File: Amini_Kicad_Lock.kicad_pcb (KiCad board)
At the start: 2 copper layers, 25.7 x 19.1 mm, 40 parts, among them J1 Conn_01x02_Pin, J2 Conn_01x04, J3 MM8130-2600RA2, J4 Conn_01x03_Pin, U1 nRF5340-QKxx, X1 32MHz, X2 32.768kHz

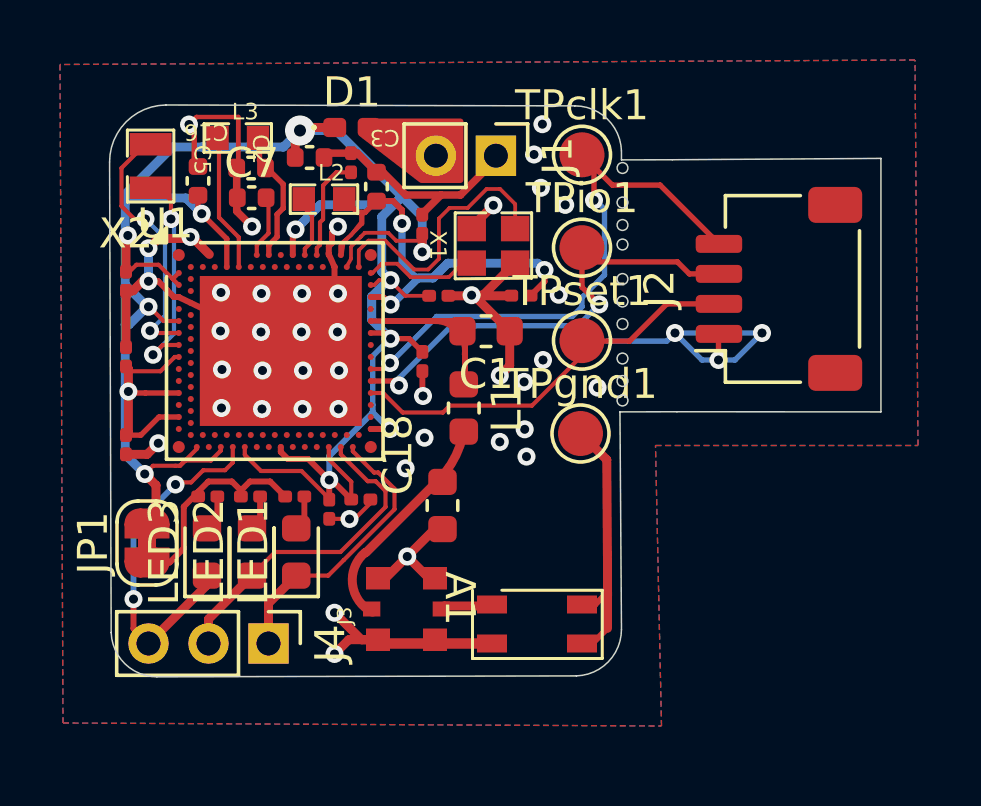
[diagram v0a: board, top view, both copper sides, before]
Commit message: New antenna design done
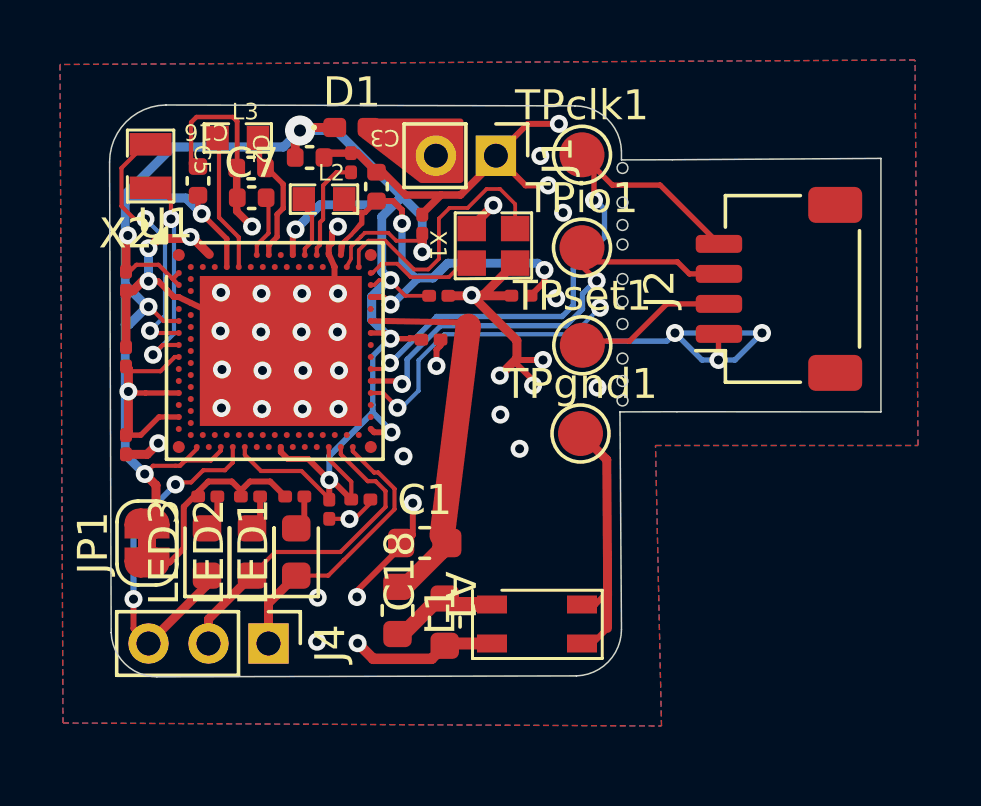
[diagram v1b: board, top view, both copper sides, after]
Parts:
- removed J3: MM8130-2600RA2, MM8130-2600RA2 antenna:MURATA_MM8130-2600RA2
- moved C1 7.35 mm to (182.2, 68.2), turned to 0 degrees
- moved L1 7.10 mm to (181.3, 70.5)
- moved C18 3.89 mm to (182.9, 70.9)
- moved C13 0.43 mm to (182.1, 61.5), turned to 0 degrees
- moved TPset1 0.16 mm to (187.5, 61.7)
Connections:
- A1 pad 1: Net-(A1-Pad1) -> Net-(C18-Pad2)
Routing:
- net GND: track 66.3 -> 70.6 mm, vias 47 -> 46
- net Net-(U1-ANT): track 0.00 -> 2.45 mm
- net Net-(A1-Pad1): track 1.75 -> 0.00 mm
- net /~{RESET}: track 13.4 -> 15.1 mm, vias 0 -> 2

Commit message: some changes done
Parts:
- removed J4: Conn_01x03_Pin, Connector_PinHeader_2.00mm:PinHeader_1x03_P2.00mm_Vertical
- added C17: 0.7pF, Capacitor_SMD:C_0402_1005Metric_Pad0.74x0.62mm_HandSolder, F.Cu at (183.4, 61.4)
- added C19: N.C., Capacitor_SMD:C_0402_1005Metric_Pad0.74x0.62mm_HandSolder, F.Cu at (185.4, 63.0)
- added J3: Conn_01x04_Pin, Connector_PinHeader_2.00mm:PinHeader_1x04_P2.00mm_Vertical, F.Cu at (180.1, 71.5)
- added L4: 2.2nH, Capacitor_SMD:C_0402_1005Metric_Pad0.74x0.62mm_HandSolder, F.Cu at (184.9, 61.2)
- C1, C18, L1: footprint Inductor_SMD:L_0603_1608Metric -> Capacitor_SMD:C_0402_1005Metric_Pad0.74x0.62mm_HandSolder
- J2: footprint Connector_JST:JST_SH_SM04B-SRSS-TB_1x04-1MP_P1.00mm_Horizontal -> Connector_PinHeader_2.54mm:PinHeader_2x02_P2.54mm_Vertical
- moved C18 3.68 mm to (182.8, 67.2), turned to 180 degrees
- moved C1 2.60 mm to (182.9, 70.8), turned to 60 degrees
- moved J2 2.11 mm to (192.1, 60.6)
- moved L1 1.90 mm to (182.2, 68.8), turned to -70 degrees
- moved C14 0.31 mm to (182.1, 59.9)
- moved C13 0.11 mm to (182.0, 61.5), turned to -90 degrees
- moved C11 0.11 mm to (179.0, 67.0)
- moved J1 0.06 mm to (184.6, 55.3)
- renumbered TPclk1 to clk, TPgnd1 to gnd, TPio1 to io, TPset1 to set
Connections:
- C1 pad 2: Net-(U1-ANT) -> Net-(C1-Pad2)
- L1 pad 1: Net-(U1-ANT) -> Net-(C1-Pad2)
- LED1 pad 1: /LED1 -> /LED3
- LED3 pad 1: /LED3 -> /LED1
- U1 pad A25: GND -> unconnected-(U1-NC-PadA25)
- U1 pad AA1: unconnected-(U1-NFC2/P0.03-PadAA1) -> /MIC
- U1 pad AE31: (no net) -> unconnected-(U1-AIN7/P0.28-PadAE31)
- U1 pad AL29: /LED1 -> /LED3
- U1 pad AL9: /LED3 -> unconnected-(U1-IO3/P0.16-PadAL9)
- U1 pad B26: GND -> unconnected-(U1-NC-PadB26)
- U1 pad G1: GND -> unconnected-(U1-NC-PadG1)
- U1 pad H2: GND -> unconnected-(U1-NC-PadH2)
- U1 pad W1: unconnected-(U1-NFC1/P0.02-PadW1) -> /LED1
- X1 pad 4: GND -> unconnected-(X1-GND-Pad4)
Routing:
- net /MIC: track 0.00 -> 10.3 mm, vias 0 -> 1
- net /~{RESET}: track 15.1 -> 25.0 mm
- net GND: track 70.6 -> 61.5 mm, vias 46 -> 41
- net /LED1: track 9.57 -> 15.5 mm, vias 0 -> 1
- net Net-(A1-Pad1): track 3.71 -> 0.00 mm
- net /SWDIO: track 15.6 -> 19.0 mm
- net /SWDCLK: track 19.2 -> 21.4 mm
- net /LED3: track 11.9 -> 10.0 mm, vias 2 -> 0
- net Net-(U1-ANT): track 2.45 -> 4.15 mm
- net VDD_nRF: track 85.5 -> 87.1 mm
- net unconnected-(X1-GND-Pad4): track 0.00 -> 1.08 mm
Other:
- board text added: "+"
- board text added: "2024 - June - v.1.0"
- board text added: "AMINI"
- board text added: "Bluetooth"
- board text added: "Lock"
- board text added: "clk"
- board text added: "gnd"
- board text added: "io"
- board text added: "set"
- board text added: "⏚"

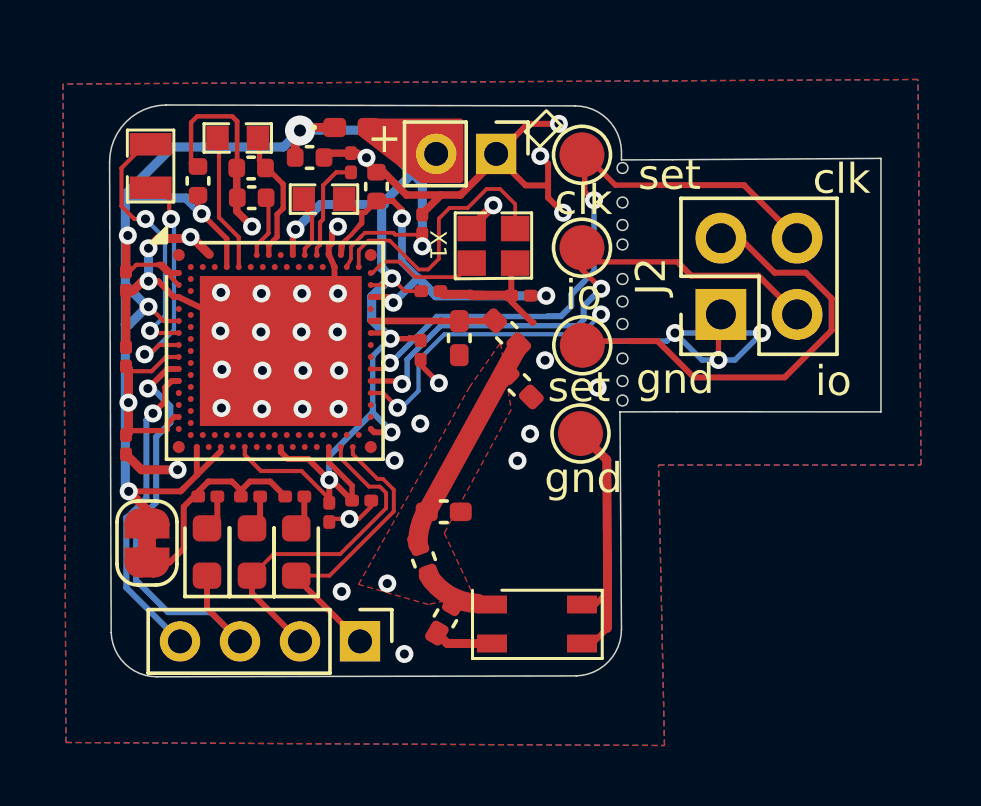
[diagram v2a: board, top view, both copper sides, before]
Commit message: fikset småting og endret logo
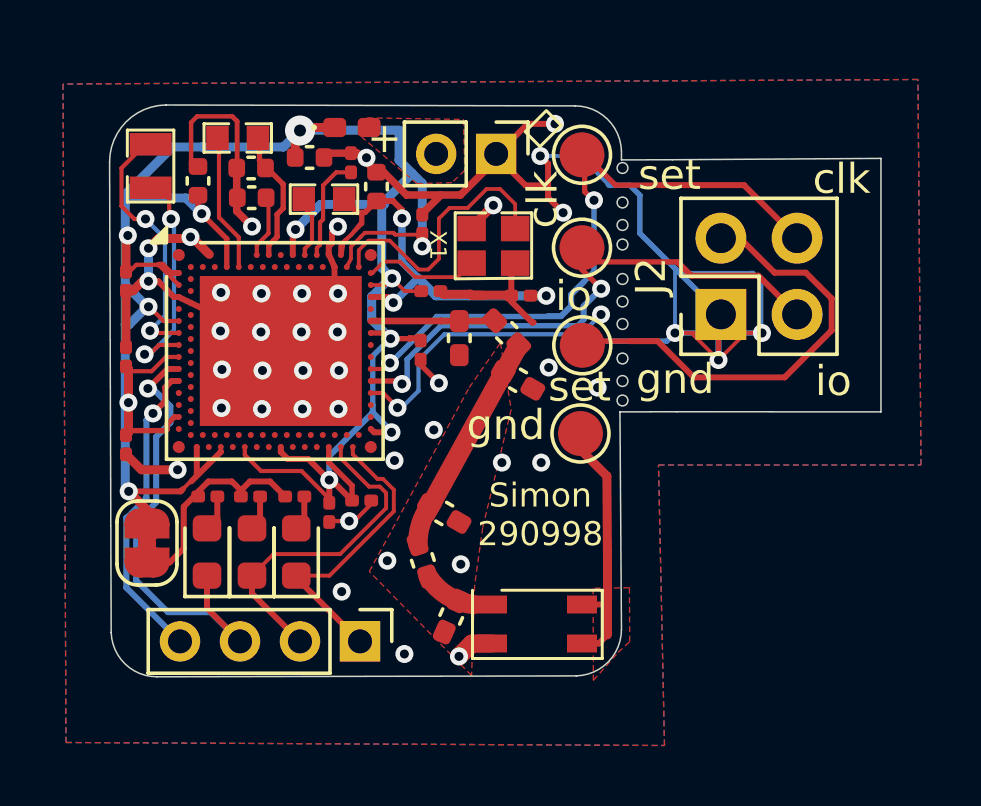
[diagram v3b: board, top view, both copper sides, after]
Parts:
- moved C1 0.20 mm to (183.1, 70.7), turned to 66 degrees
- moved C19 0.16 mm to (185.3, 62.8), turned to 150 degrees
- moved C18 0.06 mm to (182.9, 67.3), turned to 150 degrees
- turned L1 to -72 degrees
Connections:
- net Net-(D1-A) renamed /IN
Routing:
- net GND: track 61.5 -> 81.7 mm, vias 41 -> 43
- added copper zone on F.Cu, net /IN
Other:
- board text added: "2024"
- board text added: "Amini"
- board text added: "Bluetooth Lock"
- board text added: "Simon 290998"

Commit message: fikset logo, ligger igjen søkkepø
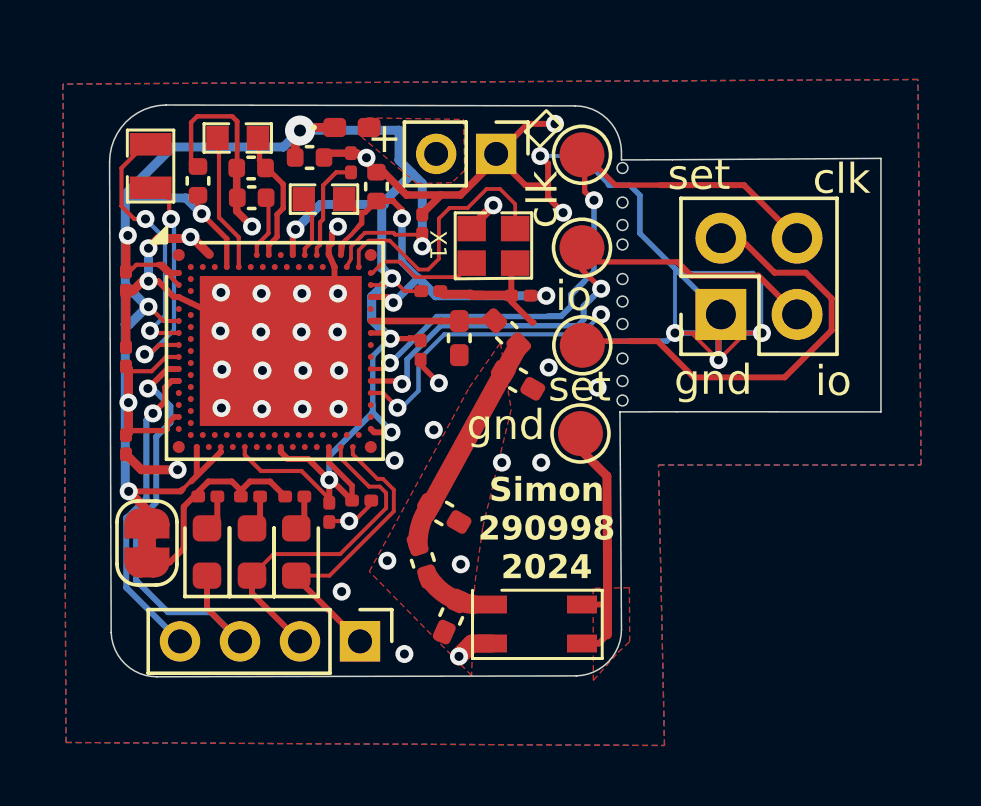
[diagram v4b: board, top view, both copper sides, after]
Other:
- board text added: "Simon 290998 2024"
- board text removed: "2024"
- board text removed: "Simon 290998"

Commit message: fikset logo, funker greit
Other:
- board text removed: "2024 - June - v.1.0"
- board text removed: "AMINI"
- board text removed: "Bluetooth"
- board text removed: "Lock"

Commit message: Trodde runde greier var hull, not hull
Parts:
- added mouse-bite-2.54mm-slot: VAL**, Mouse_Bite:mouse-bite-2.54mm-slot, F.Cu at (189.9, 60.0)
- moved J2 1.27 mm to (193.1, 61.4)
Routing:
- net GND: track 81.7 -> 56.9 mm, vias 43 -> 40
- net /~{RESET}: track 25.0 -> 18.1 mm
- net /SWDCLK: track 21.4 -> 18.5 mm
- net /SWDIO: track 19.0 -> 20.0 mm
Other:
- board size 25.7 x 19.1 mm -> 19.8 x 19.1 mm

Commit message: klar for produksjon
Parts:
- removed mouse-bite-2.54mm-slot: VAL**, Mouse_Bite:mouse-bite-2.54mm-slot
- added ?: , clipboard:7f799c2c-a0ec-4dfc-857c-f149acab8d33, F.Cu at (188.9, 59.5)
- added ?: , clipboard:7f799c2c-a0ec-4dfc-857c-f149acab8d33, F.Cu at (188.9, 58.1)
- added ?: , clipboard:7f799c2c-a0ec-4dfc-857c-f149acab8d33, F.Cu at (188.9, 60.6)
- added ?: , clipboard:7f799c2c-a0ec-4dfc-857c-f149acab8d33, F.Cu at (188.9, 55.8)
- added ?: , clipboard:7f799c2c-a0ec-4dfc-857c-f149acab8d33, F.Cu at (188.9, 57.1)
- added ?: , clipboard:7f799c2c-a0ec-4dfc-857c-f149acab8d33, F.Cu at (189.0, 61.8)
- moved J2 2.01 mm to (191.6, 60.0)
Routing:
- net GND: track 56.9 -> 76.3 mm, vias 40 -> 42
- net /SWDCLK: track 18.5 -> 21.6 mm
- net /SWDIO: track 20.0 -> 18.3 mm
- net /~{RESET}: track 18.1 -> 18.6 mm, vias 2 -> 4
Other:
- board size 19.8 x 19.1 mm -> 24.5 x 19.1 mm

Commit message: Produsert
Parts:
- C1: value 0.7pF -> 0
- C18: value N.C. -> 0
- L1: value 2.2nH -> 0r
- moved ? 0.20 mm to (188.9, 57.3)
- moved ? 0.08 mm to (188.9, 60.5)
- moved ? 0.08 mm to (188.9, 55.9)
- moved ? 0.07 mm to (188.9, 59.6)
- moved ? 0.06 mm to (188.9, 58.2)
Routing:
- net GND: track 76.3 -> 74.3 mm, vias 42 -> 44
- net /~{RESET}: track 18.6 -> 18.1 mm
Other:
- board text added: "Simon 290998 210624"
- board text removed: "Simon 290998 2024"
